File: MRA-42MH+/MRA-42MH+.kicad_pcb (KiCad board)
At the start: 2 copper layers, 60 x 30 mm, 191 parts, among them P1 CONN_01X02, U1 MRA-42MH+, X1 SMA-F, X2 SMA-F, X3 SMA-F

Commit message: Removed some missplaced vias
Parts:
- removed REF**23112, REF**23113, REF**23114, REF**23115, REF**2312, REF**2313, REF**2314, REF**2315: VIA-0.3, JueVias:VIA-0.3
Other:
- board text added: "L13 Mixer IP3 (OUT): 24dBm LO/RF: 1000..4200, IF: 10..800"
- board text removed: "L13 Mixer IP3 (OUT): 26dBm LO/RF: 1000..4200, IF: 10..800"
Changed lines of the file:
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@@
 (kicad_pcb (version 4) (host pcbnew 4.0.2+e4-6225~38~ubuntu15.10.1-stable)
   (general
-    (links 191)
-    (no_connects 35)
-    (area 89.924999 89.924999 150.075001 120.075001)
+    (links 208)
+    (no_connects 4)
+    (area 82.392143 88.485 180.225002 1121.34)
     (thickness 1.6)
     (drawings 12)
     (tracks 35)
     (zones 0)
-    (modules 191)
+    (modules 183)
     (nets 10)
   )
@@
   )
   (module JueVias:VIA-0.3 (layer B.Cu)
-    (at 126.096 1119.095)
-    (fp_text reference REF**23115 (at 0 1.27) (layer B.SilkS) hide
-      (effects (font (size 1 1) (thickness 0.15)) (justify mirror))
-    )
-    (fp_text value VIA-0.3 (at 0 -1.397) (layer B.Fab) hide
-      (effects (font (size 1 1) (thickness 0.15)) (justify mirror))
-    )
-    (pad 1 thru_hole circle (at 0 0) (size 0.6 0.6) (drill 0.3) (layers *.Cu)
-      (net 1 GNDA))
-  )
-  (module JueVias:VIA-0.3 (layer B.Cu)
-    (at 126.096 865.095)
-    (fp_text reference REF**23114 (at 0 1.27) (layer B.SilkS) hide
-      (effects (font (size 1 1) (thickness 0.15)) (justify mirror))
-    )
-    (fp_text value VIA-0.3 (at 0 -1.397) (layer B.Fab) hide
-      (effects (font (size 1 1) (thickness 0.15)) (justify mirror))
-    )
-    (pad 1 thru_hole circle (at 0 0) (size 0.6 0.6) (drill 0.3) (layers *.Cu)
-      (net 1 GNDA))
-  )
-  (module JueVias:VIA-0.3 (layer B.Cu)
-    (at 126.096 611.095)
-    (fp_text reference REF**23113 (at 0 1.27) (layer B.SilkS) hide
-      (effects (font (size 1 1) (thickness 0.15)) (justify mirror))
-    )
-    (fp_text value VIA-0.3 (at 0 -1.397) (layer B.Fab) hide
-      (effects (font (size 1 1) (thickness 0.15)) (justify mirror))
-    )
-    (pad 1 thru_hole circle (at 0 0) (size 0.6 0.6) (drill 0.3) (layers *.Cu)
-      (net 1 GNDA))
-  )
-  (module JueVias:VIA-0.3 (layer B.Cu)
-    (at 126.096 357.095)
-    (fp_text reference REF**23112 (at 0 1.27) (layer B.SilkS) hide
-      (effects (font (size 1 1) (thickness 0.15)) (justify mirror))
-    )
-    (fp_text value VIA-0.3 (at 0 -1.397) (layer B.Fab) hide
-      (effects (font (size 1 1) (thickness 0.15)) (justify mirror))
-    )
-    (pad 1 thru_hole circle (at 0 0) (size 0.6 0.6) (drill 0.3) (layers *.Cu)
-      (net 1 GNDA))
-  )
-  (module JueVias:VIA-0.3 (layer B.Cu)
-    (at 126.096 1119.095)
-    (fp_text reference REF**2315 (at 0 1.27) (layer B.SilkS) hide
-      (effects (font (size 1 1) (thickness 0.15)) (justify mirror))
-    )
-    (fp_text value VIA-0.3 (at 0 -1.397) (layer B.Fab) hide
-      (effects (font (size 1 1) (thickness 0.15)) (justify mirror))
-    )
-    (pad 1 thru_hole circle (at 0 0) (size 0.6 0.6) (drill 0.3) (layers *.Cu)
-      (net 1 GNDA))
-  )
-  (module JueVias:VIA-0.3 (layer B.Cu)
-    (at 126.096 865.095)
-    (fp_text reference REF**2314 (at 0 1.27) (layer B.SilkS) hide
-      (effects (font (size 1 1) (thickness 0.15)) (justify mirror))
-    )
-    (fp_text value VIA-0.3 (at 0 -1.397) (layer B.Fab) hide
-      (effects (font (size 1 1) (thickness 0.15)) (justify mirror))
-    )
-    (pad 1 thru_hole circle (at 0 0) (size 0.6 0.6) (drill 0.3) (layers *.Cu)
-      (net 1 GNDA))
-  )
-  (module JueVias:VIA-0.3 (layer B.Cu)
-    (at 126.096 611.095)
-    (fp_text reference REF**2313 (at 0 1.27) (layer B.SilkS) hide
-      (effects (font (size 1 1) (thickness 0.15)) (justify mirror))
-    )
-    (fp_text value VIA-0.3 (at 0 -1.397) (layer B.Fab) hide
-      (effects (font (size 1 1) (thickness 0.15)) (justify mirror))
-    )
-    (pad 1 thru_hole circle (at 0 0) (size 0.6 0.6) (drill 0.3) (layers *.Cu)
-      (net 1 GNDA))
-  )
-  (module JueVias:VIA-0.3 (layer B.Cu)
-    (at 126.096 357.095)
-    (fp_text reference REF**2312 (at 0 1.27) (layer B.SilkS) hide
-      (effects (font (size 1 1) (thickness 0.15)) (justify mirror))
-    )
-    (fp_text value VIA-0.3 (at 0 -1.397) (layer B.Fab) hide
-      (effects (font (size 1 1) (thickness 0.15)) (justify mirror))
-    )
-    (pad 1 thru_hole circle (at 0 0) (size 0.6 0.6) (drill 0.3) (layers *.Cu)
-      (net 1 GNDA))
-  )
-  (module JueVias:VIA-0.3 (layer B.Cu)
     (at 126.096 103.73)
     (fp_text reference REF**23111 (at 0 1.27) (layer B.SilkS) hide
@@
     (effects (font (size 1.5 1.5) (thickness 0.3)) (justify right))
   )
-  (gr_text "L13 Mixer    IP3 (OUT): 26dBm\nLO/RF: 1000..4200, IF: 10..800" (at 116.444 94.332) (layer F.SilkS)
+  (gr_text "L13 Mixer    IP3 (OUT): 24dBm\nLO/RF: 1000..4200, IF: 10..800" (at 116.444 94.332) (layer F.SilkS)
     (effects (font (size 1 1) (thickness 0.15)) (justify left))
   )

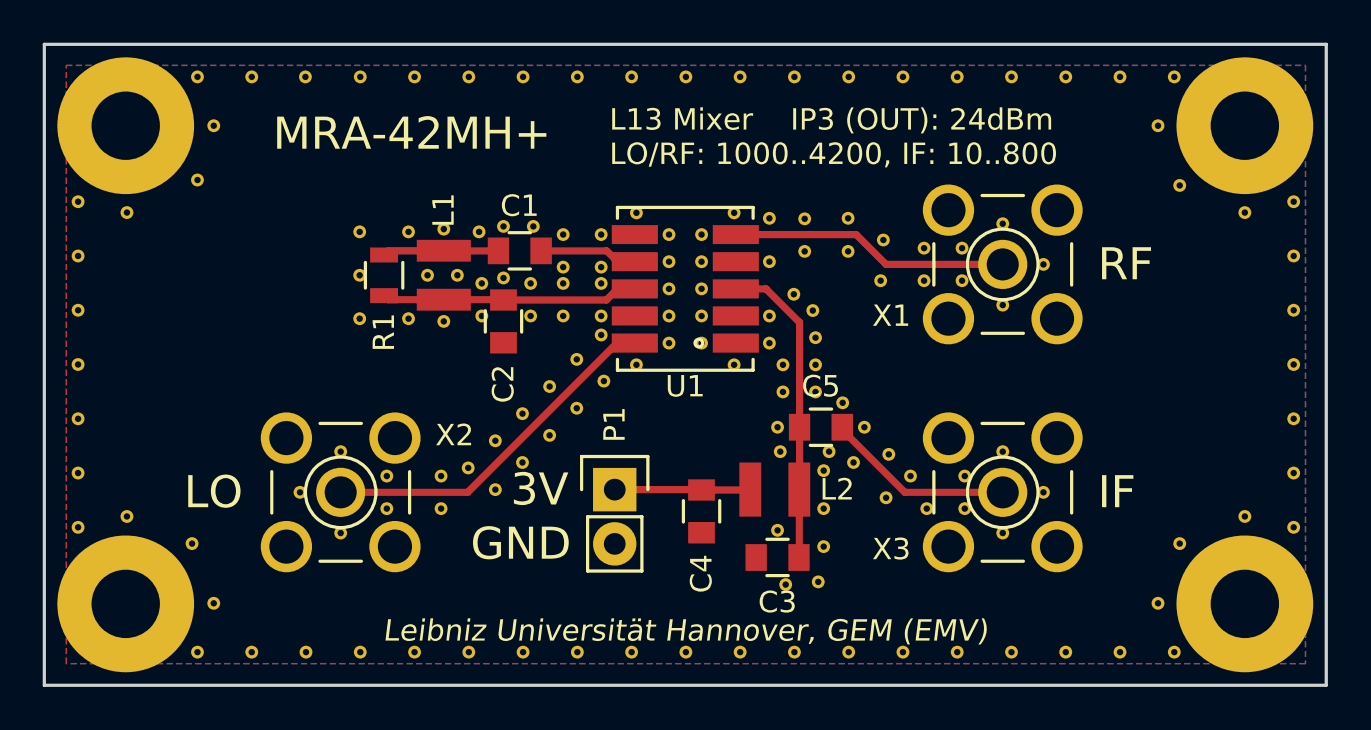
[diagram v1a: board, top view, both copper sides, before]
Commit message: MRA-42MH+: corrected 50Ohm CPW, new VIA arrangement
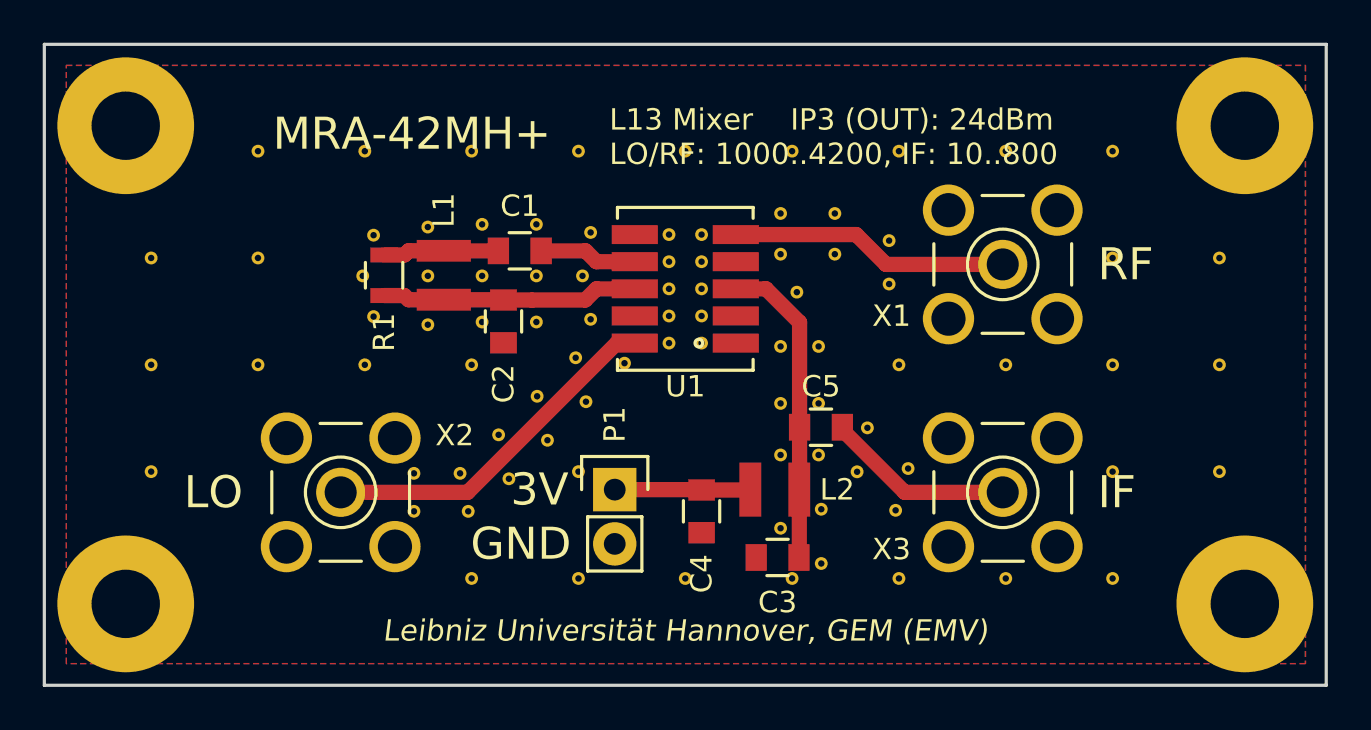
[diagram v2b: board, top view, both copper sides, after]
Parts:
- removed REF**211 (x2), REF**2111 (x8), REF**2112 (x2), REF**2113 (x2), REF**2114 (x2), REF**2115 (x2), REF**2116 (x2), REF**2117 (x8), REF**221 (x2), REF**23111 (x25), REF**241 (x2), REF**251 (x2), REF**261 (x2), REF**2711 (x2), REF**2721 (x2), REF**2731 (x2), REF**2741 (x2), REF**2751 (x2), REF**2761 (x2), REF**27711 (x2), REF**27721 (x2), REF**27731 (x2), REF**27741 (x2), REF**27751 (x2), REF**27761 (x2), REF**27771 (x2): VIA-0.3, JueVias:VIA-0.3
- removed the REF**231 at (134.9, 112.9)
- removed the REF**231 at (125.6, 99.7)
- removed the REF**231 at (131.2, 99.5)
- removed the REF**231 at (133.0, 101.1)
- removed the REF**231 at (129.3, 99.2)
- removed the REF**231 at (129.1, 101.1)
- removed the REF**231 at (131.2, 101.1)
- removed the REF**231 at (127.6, 99.7)
- removed the REF**231 at (127.6, 98.1)
- removed the REF**231 at (109.3, 100.8)
- removed the REF**231 at (107.9, 100.8)
- removed the REF**231 at (136.8, 111.0)
- removed the REF**231 at (112.9, 98.5)
- removed the REF**231 at (108.7, 103.0)
- removed the REF**231 at (107.0, 102.8)
- removed the REF**231 at (104.8, 102.8)
- removed the REF**231 at (104.8, 100.8)
- removed the REF**231 at (104.8, 98.8)
- removed the REF**231 at (107.0, 98.8)
- removed the REF**231 at (108.7, 98.7)
- removed the REF**231 at (110.3, 98.8)
- removed the REF**231 at (111.5, 98.5)
- removed the REF**231 at (134.9, 109.1)
- removed the REF**231 at (111.5, 100.9)
- removed the REF**231 at (110.5, 102.7)
- removed the REF**231 at (110.5, 101.2)
- removed the REF**231 at (112.8, 102.7)
- removed the REF**231 at (112.8, 101.2)
- removed the REF**231 at (116.1, 102.7)
- removed the REF**231 at (114.3, 102.7)
- removed the REF**231 at (116.1, 101.2)
- removed the REF**231 at (114.3, 101.2)
- removed the REF**231 at (116.1, 100.4)
- removed the REF**231 at (136.8, 100.3)
- removed the REF**231 at (114.3, 100.4)
- removed the REF**231 at (114.3, 98.9)
- removed the REF**231 at (122.3, 105.0)
- removed the REF**231 at (122.3, 97.9)
- removed the REF**231 at (117.7, 97.9)
- removed the REF**231 at (103.9, 112.9)
- removed the REF**231 at (102.0, 111.0)
- removed the REF**231 at (103.9, 109.1)
- removed the REF**231 at (123.9, 104.0)
- removed the REF**231 at (123.9, 102.7)
- removed the REF**231 at (134.9, 102.2)
- removed the REF**231 at (123.9, 100.2)
- removed the REF**231 at (116.1, 98.9)
- removed the REF**231 at (134.9, 98.4)
- removed the REF**231 at (117.7, 105.0)
- removed the REF**231 at (116.1, 103.6)
- removed the REF**231 at (111.1, 110.8)
- removed the REF**231 at (112.4, 109.6)
- removed the REF**231 at (113.7, 108.3)
- removed the REF**231 at (114.9, 107.0)
- removed the REF**231 at (116.2, 105.8)
- removed the REF**231 at (114.9, 104.7)
- removed the REF**231 at (133.0, 99.5)
- removed the REF**231 at (113.7, 106.0)
- removed the REF**231 at (112.4, 107.3)
- removed the REF**231 at (111.1, 108.6)
- removed the REF**231 at (109.8, 109.8)
- removed the REF**231 at (108.6, 110.2)
- removed the REF**231 at (106.0, 110.2)
- removed the REF**231 at (106.0, 111.7)
- removed the REF**231 at (108.6, 111.7)
- removed the REF**231 at (102.2, 118.4)
- removed the REF**231 at (102.2, 91.5)
- removed the REF**231 at (123.9, 98.1)
- removed the REF**231 at (125.6, 98.2)
- added REF**2311: VIA-0.3, JueVias:VIA-0.3, F.Cu at (107.3, 111.9)
- added REF**2311: VIA-0.3, JueVias:VIA-0.3, F.Cu at (107.3, 110.1)
- added REF**2321: VIA-0.3, JueVias:VIA-0.3, F.Cu at (109.8, 111.9)
- added REF**23211: VIA-0.3, JueVias:VIA-0.3, F.Cu at (109.5, 110.1)
- added REF**232111: VIA-0.3, JueVias:VIA-0.3, F.Cu at (111.7, 110.3)
- added REF**232122: VIA-0.3, JueVias:VIA-0.3, F.Cu at (113.5, 108.5)
- added REF**232133: VIA-0.3, JueVias:VIA-0.3, F.Cu at (115.4, 106.7)
- added REF**23214102: VIA-0.3, JueVias:VIA-0.3, F.Cu at (135.0, 95.0)
- added REF**23214104: VIA-0.3, JueVias:VIA-0.3, F.Cu at (135.0, 105.0)
- added REF**23214106: VIA-0.3, JueVias:VIA-0.3, F.Cu at (135.0, 115.0)
- added REF**23214112: VIA-0.3, JueVias:VIA-0.3, F.Cu at (140.0, 95.0)
- added REF**23214113: VIA-0.3, JueVias:VIA-0.3, F.Cu at (140.0, 100.0)
- added REF**23214114: VIA-0.3, JueVias:VIA-0.3, F.Cu at (140.0, 105.0)
- added REF**23214115: VIA-0.3, JueVias:VIA-0.3, F.Cu at (140.0, 110.0)
- added REF**23214116: VIA-0.3, JueVias:VIA-0.3, F.Cu at (140.0, 115.0)
- added REF**23214123: VIA-0.3, JueVias:VIA-0.3, F.Cu at (145.0, 100.0)
- added REF**23214124: VIA-0.3, JueVias:VIA-0.3, F.Cu at (145.0, 105.0)
- added REF**23214125: VIA-0.3, JueVias:VIA-0.3, F.Cu at (145.0, 110.0)
- added REF**2321423: VIA-0.3, JueVias:VIA-0.3, F.Cu at (95.0, 100.0)
- added REF**2321424: VIA-0.3, JueVias:VIA-0.3, F.Cu at (95.0, 105.0)
- added REF**2321425: VIA-0.3, JueVias:VIA-0.3, F.Cu at (95.0, 110.0)
- added REF**2321432: VIA-0.3, JueVias:VIA-0.3, F.Cu at (100.0, 95.0)
- added REF**2321433: VIA-0.3, JueVias:VIA-0.3, F.Cu at (100.0, 100.0)
- added REF**2321434: VIA-0.3, JueVias:VIA-0.3, F.Cu at (100.0, 105.0)
- added REF**232144: VIA-0.3, JueVias:VIA-0.3, F.Cu at (125.2, 101.6)
- added REF**232144: VIA-0.3, JueVias:VIA-0.3, F.Cu at (126.2, 104.1)
- added REF**232144: VIA-0.3, JueVias:VIA-0.3, F.Cu at (104.9, 100.8)
- added REF**232144: VIA-0.3, JueVias:VIA-0.3, F.Cu at (115.2, 100.8)
- added REF**232144: VIA-0.3, JueVias:VIA-0.3, F.Cu at (113.0, 100.8)
- added REF**232144: VIA-0.3, JueVias:VIA-0.3, F.Cu at (110.5, 100.8)
- added REF**232144: VIA-0.3, JueVias:VIA-0.3, F.Cu at (108.0, 100.8)
- added REF**232144: VIA-0.3, JueVias:VIA-0.3, F.Cu at (115.6, 102.9)
- added REF**232144: VIA-0.3, JueVias:VIA-0.3, F.Cu at (113.0, 103.0)
- added REF**232144: VIA-0.3, JueVias:VIA-0.3, F.Cu at (110.5, 103.0)
- added REF**232144: VIA-0.3, JueVias:VIA-0.3, F.Cu at (108.0, 103.1)
- added REF**232144: VIA-0.3, JueVias:VIA-0.3, F.Cu at (124.5, 112.6)
- added REF**232144: VIA-0.3, JueVias:VIA-0.3, F.Cu at (105.4, 102.7)
- added REF**232144: VIA-0.3, JueVias:VIA-0.3, F.Cu at (105.4, 98.9)
- added REF**232144: VIA-0.3, JueVias:VIA-0.3, F.Cu at (108.0, 98.6)
- added REF**232144: VIA-0.3, JueVias:VIA-0.3, F.Cu at (110.5, 98.4)
- added REF**232144: VIA-0.3, JueVias:VIA-0.3, F.Cu at (113.0, 98.4)
- added REF**232144: VIA-0.3, JueVias:VIA-0.3, F.Cu at (115.6, 98.8)
- added REF**232144: VIA-0.3, JueVias:VIA-0.3, F.Cu at (130.4, 109.9)
- added REF**232144: VIA-0.3, JueVias:VIA-0.3, F.Cu at (129.5, 101.2)
- added REF**232144: VIA-0.3, JueVias:VIA-0.3, F.Cu at (127.0, 99.8)
- added REF**232144: VIA-0.3, JueVias:VIA-0.3, F.Cu at (124.5, 99.8)
- added REF**232144: VIA-0.3, JueVias:VIA-0.3, F.Cu at (126.4, 114.3)
- added REF**232144: VIA-0.3, JueVias:VIA-0.3, F.Cu at (129.5, 99.2)
- added REF**232144: VIA-0.3, JueVias:VIA-0.3, F.Cu at (127.0, 97.9)
- added REF**232144: VIA-0.3, JueVias:VIA-0.3, F.Cu at (124.5, 97.9)
- added REF**232144: VIA-0.3, JueVias:VIA-0.3, F.Cu at (128.5, 108.0)
- added REF**232144: VIA-0.3, JueVias:VIA-0.3, F.Cu at (129.8, 111.8)
- added REF**232144: VIA-0.3, JueVias:VIA-0.3, F.Cu at (128.0, 110.0)
- added REF**232144: VIA-0.3, JueVias:VIA-0.3, F.Cu at (117.2, 104.9)
- added REF**232144: VIA-0.3, JueVias:VIA-0.3, F.Cu at (126.4, 111.8)
- added REF**232144: VIA-0.3, JueVias:VIA-0.3, F.Cu at (126.2, 109.2)
- added REF**232144: VIA-0.3, JueVias:VIA-0.3, F.Cu at (124.5, 109.2)
- added REF**232144: VIA-0.3, JueVias:VIA-0.3, F.Cu at (124.5, 106.8)
- added REF**232144: VIA-0.3, JueVias:VIA-0.3, F.Cu at (124.5, 104.1)
- added REF**232144: VIA-0.3, JueVias:VIA-0.3, F.Cu at (126.2, 106.8)
- added REF**2321442: VIA-0.3, JueVias:VIA-0.3, F.Cu at (105.0, 95.0)
- added REF**2321444: VIA-0.3, JueVias:VIA-0.3, F.Cu at (105.0, 105.0)
- added REF**2321452: VIA-0.3, JueVias:VIA-0.3, F.Cu at (110.0, 95.0)
- added REF**2321454: VIA-0.3, JueVias:VIA-0.3, F.Cu at (110.0, 105.0)
- added REF**2321456: VIA-0.3, JueVias:VIA-0.3, F.Cu at (110.0, 115.0)
- added REF**2321462: VIA-0.3, JueVias:VIA-0.3, F.Cu at (115.0, 95.0)
- added REF**2321465: VIA-0.3, JueVias:VIA-0.3, F.Cu at (115.0, 110.0)
- added REF**2321466: VIA-0.3, JueVias:VIA-0.3, F.Cu at (115.0, 115.0)
- added REF**2321472: VIA-0.3, JueVias:VIA-0.3, F.Cu at (120.0, 95.0)
- added REF**2321476: VIA-0.3, JueVias:VIA-0.3, F.Cu at (120.0, 115.0)
- added REF**2321482: VIA-0.3, JueVias:VIA-0.3, F.Cu at (125.0, 95.0)
- added REF**2321486: VIA-0.3, JueVias:VIA-0.3, F.Cu at (125.0, 115.0)
- added REF**2321492: VIA-0.3, JueVias:VIA-0.3, F.Cu at (130.0, 95.0)
- added REF**2321494: VIA-0.3, JueVias:VIA-0.3, F.Cu at (130.0, 105.0)
- added REF**2321496: VIA-0.3, JueVias:VIA-0.3, F.Cu at (130.0, 115.0)
- added REF**23222: VIA-0.3, JueVias:VIA-0.3, F.Cu at (111.3, 108.3)
- added REF**23233: VIA-0.3, JueVias:VIA-0.3, F.Cu at (113.1, 106.5)
- added REF**23244: VIA-0.3, JueVias:VIA-0.3, F.Cu at (114.9, 104.7)
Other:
- net class 50Ohm: clearance 0.2 -> 0.15; trace_width 0.336 -> 0.714
- net class Default: clearance 0.1 -> 0.15
- rule trace_clearance: 0.1 -> 0.15

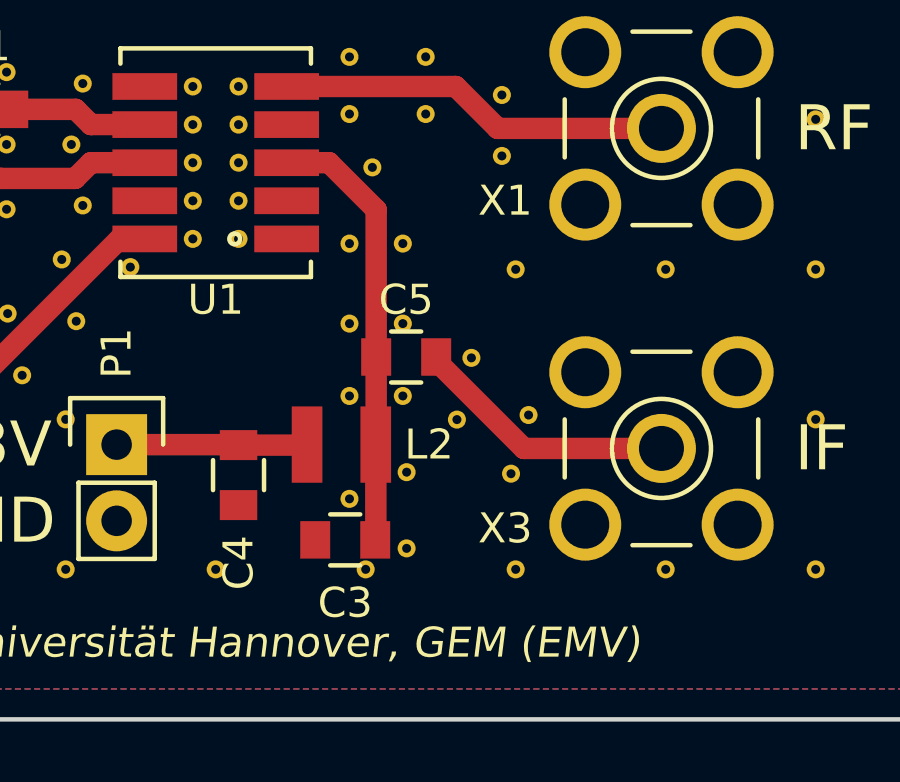
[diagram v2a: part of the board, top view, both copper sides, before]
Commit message: MRA-42MH+: Updated layout according Testboard
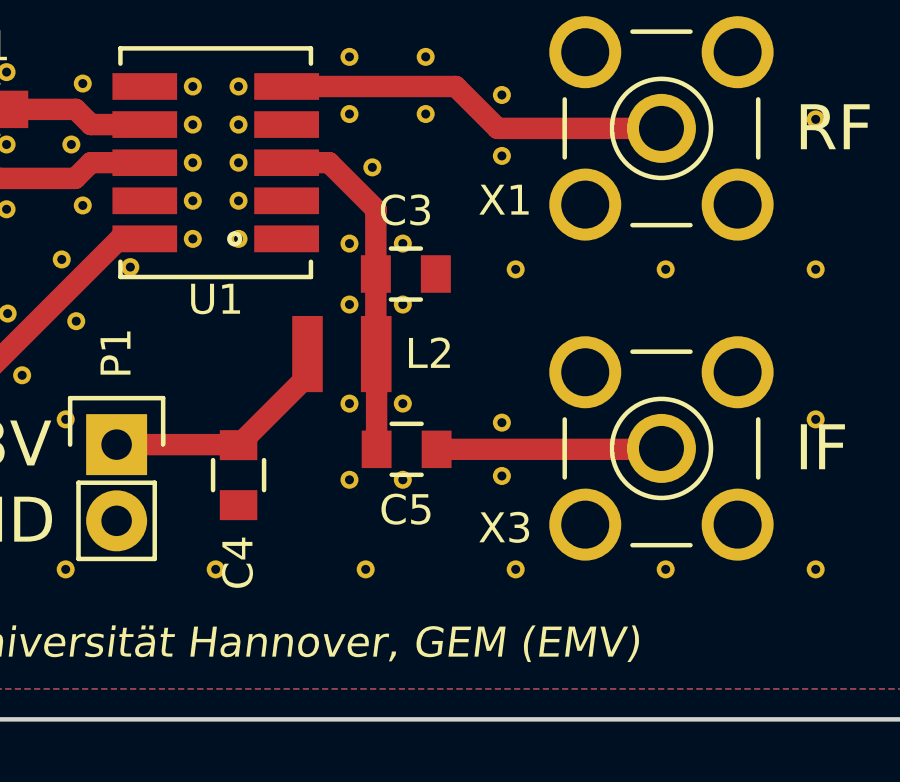
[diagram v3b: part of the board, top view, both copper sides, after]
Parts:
- removed the REF**232144 at (128.5, 108.0)
- removed the REF**232144 at (129.8, 111.8)
- removed the REF**232144 at (128.0, 110.0)
- removed the REF**232144 at (126.4, 111.8)
- added REF**232144: VIA-0.3, JueVias:VIA-0.3, F.Cu at (129.5, 111.9)
- moved C3 9.09 mm to (126.3, 105.2), turned to 0 degrees
- moved C5 3.08 mm to (126.4, 111.0)
- moved L2 3.02 mm to (124.2, 107.8)
- moved REF**232144 2.29 mm to (126.2, 112.0)
- moved REF**232144 0.92 mm to (129.5, 110.1)
- moved REF**232144 0.64 mm to (124.5, 112.0)
- moved REF**232144 0.64 mm to (124.5, 106.2)
- moved REF**232144 0.64 mm to (126.2, 106.2)
- moved REF**232144 0.25 mm to (126.2, 109.5)
- moved REF**232144 0.25 mm to (124.5, 109.5)
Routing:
- net Net-(C3-Pad1): track 14.6 -> 11.6 mm
- net +3V3: track 6.36 -> 8.06 mm
- net Net-(C5-Pad1): track 8.72 -> 7.51 mm
